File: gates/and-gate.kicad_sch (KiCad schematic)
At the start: 7 parts, among them Q19 NPN, Q20 NPN, Q21 NPN

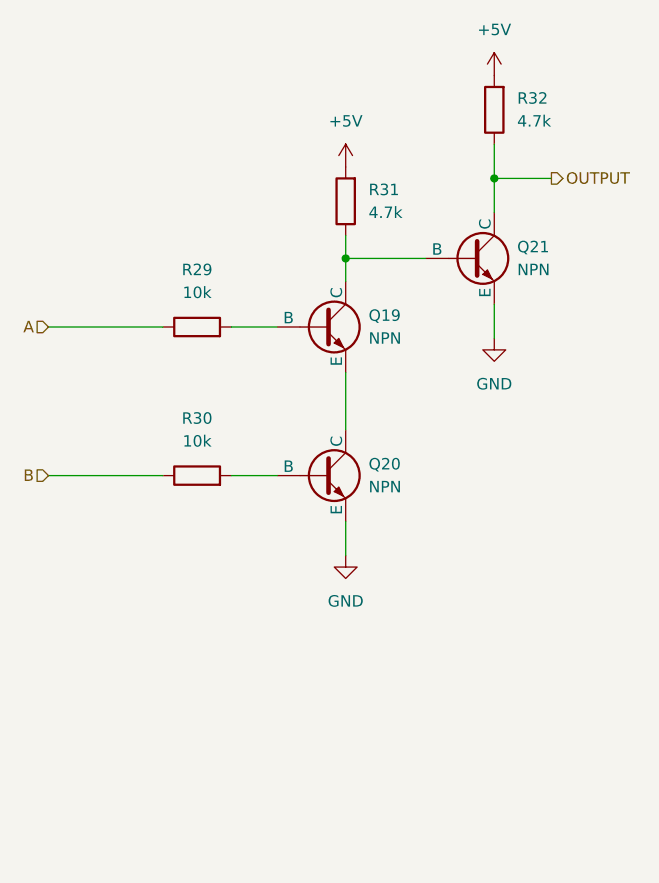
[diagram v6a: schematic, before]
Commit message: Assign footprints in half adder
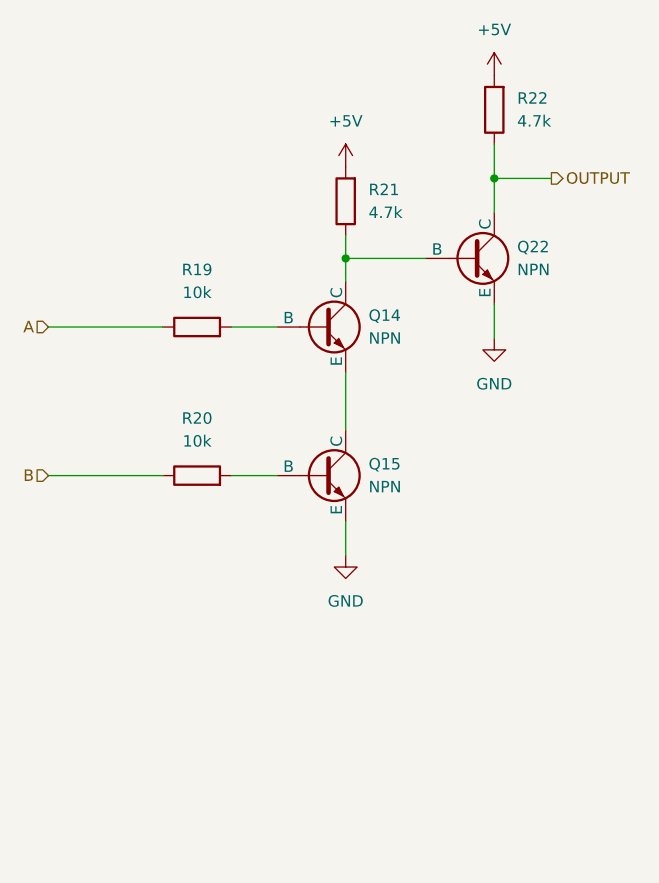
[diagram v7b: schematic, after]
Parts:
- Q14: renamed from Q19; footprint (none) -> SOT-23-3_L2.9-W1.6-P1.90-LS2.8-BR:SOT-23-3_L2.9-W1.6-P1.90-LS2.8-BR
- Q15: renamed from Q20; footprint (none) -> SOT-23-3_L2.9-W1.6-P1.90-LS2.8-BR:SOT-23-3_L2.9-W1.6-P1.90-LS2.8-BR
- Q22: renamed from Q21; footprint (none) -> SOT-23-3_L2.9-W1.6-P1.90-LS2.8-BR:SOT-23-3_L2.9-W1.6-P1.90-LS2.8-BR
- R19: renamed from R29; footprint (none) -> R0603:R0603
- R20: renamed from R30; footprint (none) -> R0603:R0603
- R21: renamed from R31; footprint (none) -> R0603:R0603
- R22: renamed from R32; footprint (none) -> R0603:R0603

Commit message: complete 2-bit encoder
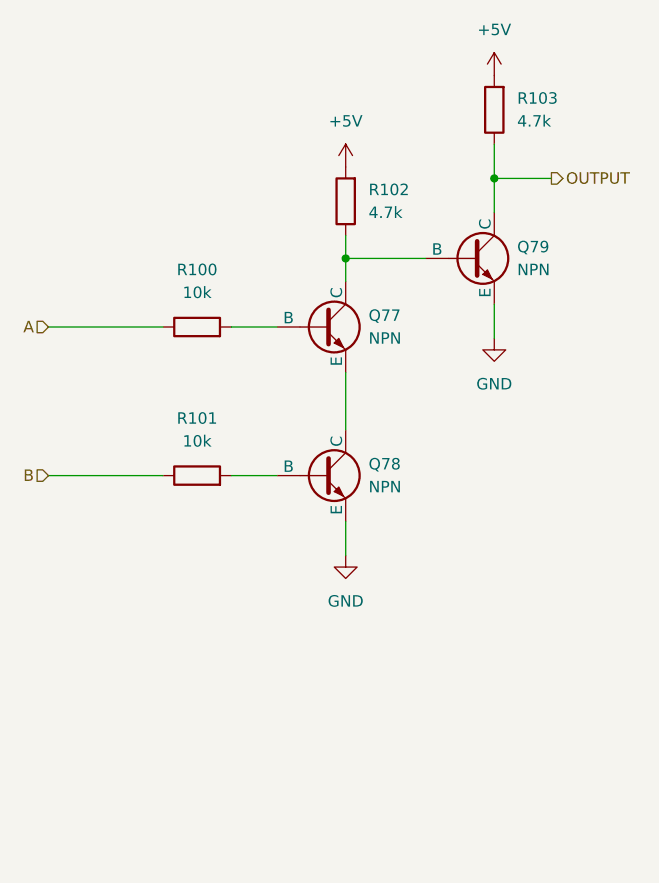
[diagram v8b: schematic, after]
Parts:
- renumbered Q14 to Q77, Q15 to Q78, Q22 to Q79, R19 to R100, R20 to R101, R21 to R102, R22 to R103
